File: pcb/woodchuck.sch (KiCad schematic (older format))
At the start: 5 parts, among them IC101 ADP3335, P101 CONN_01X02

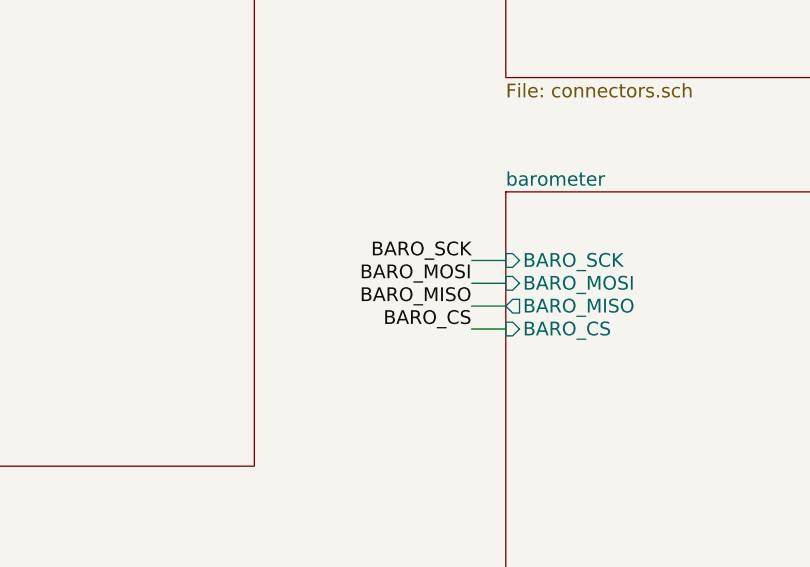
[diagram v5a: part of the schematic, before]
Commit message: Fix barometer hierarchical pins and add Farnell numbers to components
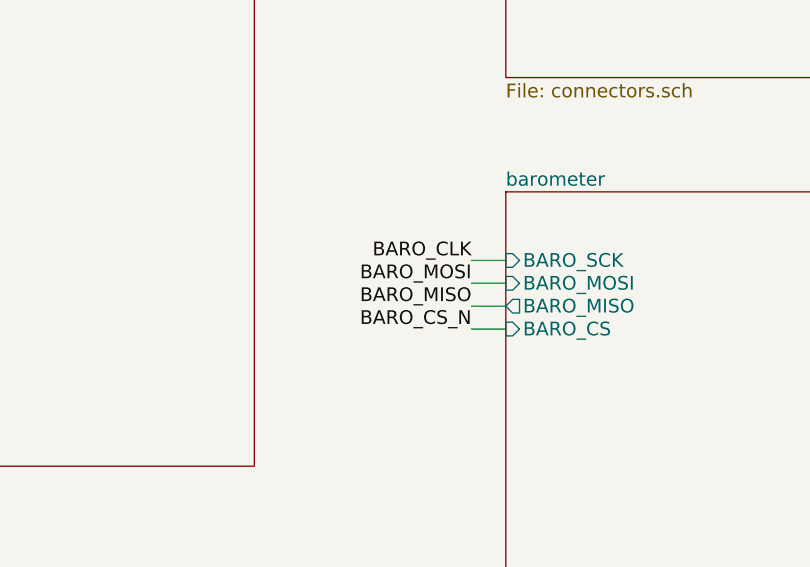
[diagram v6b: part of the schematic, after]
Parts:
- C101, C103: Farnell Value -> 2211185
- C102: Farnell Value -> 1759088
- IC101: Digikey (none) -> Value; Farnell (none) -> 2067775; Fieldname (none) -> Value
- P101: Digikey (none) -> Value; Farnell (none) -> 1830747; Fieldname (none) -> Value
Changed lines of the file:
@@
 F 2 "Woodchuck:MSOP8" H 5200 6850 60  0000 C CNN
 F 3 "" H 5600 6150 60  0000 C CNN
+F 4 "Value" H 5200 6550 60  0001 C CNN "Digikey"
+F 5 "2067775" H 5200 6550 60  0001 C CNN "Farnell"
+F 6 "Value" H 5200 6550 60  0001 C CNN "Fieldname"
 	1    5200 6550
 	1    0    0    -1
@@
 F 3 "" H 5850 6700 60  0000 C CNN
 F 4 "Value" H 5850 6700 60  0001 C CNN "Digikey"
-F 5 "Value" H 5850 6700 60  0001 C CNN "Farnell"
+F 5 "1759088" H 5850 6700 60  0001 C CNN "Farnell"
 F 6 "Value" H 5850 6700 60  0001 C CNN "Fieldname"
 	1    5850 6700
@@
 F 3 "" H 6100 6700 60  0000 C CNN
 F 4 "Value" H 6100 6700 60  0001 C CNN "Digikey"
-F 5 "Value" H 6100 6700 60  0001 C CNN "Farnell"
+F 5 "2211185" H 6100 6700 60  0001 C CNN "Farnell"
 F 6 "Value" H 6100 6700 60  0001 C CNN "Fieldname"
 	1    6100 6700
@@
 F 3 "" H 4400 6700 60  0000 C CNN
 F 4 "Value" H 4400 6700 60  0001 C CNN "Digikey"
-F 5 "Value" H 4400 6700 60  0001 C CNN "Farnell"
+F 5 "2211185" H 4400 6700 60  0001 C CNN "Farnell"
 F 6 "Value" H 4400 6700 60  0001 C CNN "Fieldname"
 	1    4400 6700
@@
 F 2 "Woodchuck:S02B-PASK-2" V 4250 6650 60  0000 C CNN
 F 3 "" H 4000 6700 60  0000 C CNN
+F 4 "Value" H 4000 6700 60  0001 C CNN "Digikey"
+F 5 "1830747" H 4000 6700 60  0001 C CNN "Farnell"
+F 6 "Value" H 4000 6700 60  0001 C CNN "Fieldname"
 	1    4000 6700
 	-1   0    0    1
@@
 	7400 4600 7250 4600
 Text Label 7250 4300 2    60   ~ 0
-BARO_SCK
+BARO_CLK
 Text Label 7250 4400 2    60   ~ 0
 BARO_MOSI
@@
 BARO_MISO
 Text Label 7250 4600 2    60   ~ 0
-BARO_CS
+BARO_CS_N
 $EndSCHEMATC

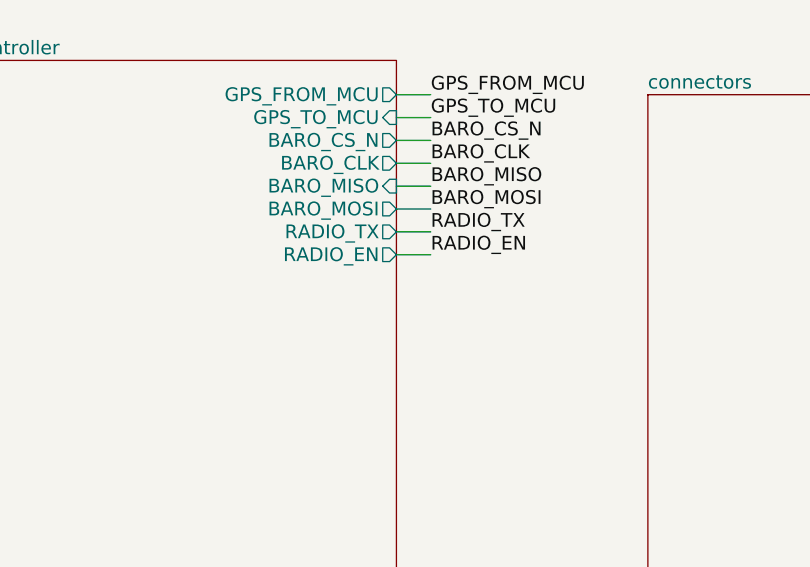
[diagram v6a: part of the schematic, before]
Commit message: Connect MTX2 parallel channel select pins to the MCU
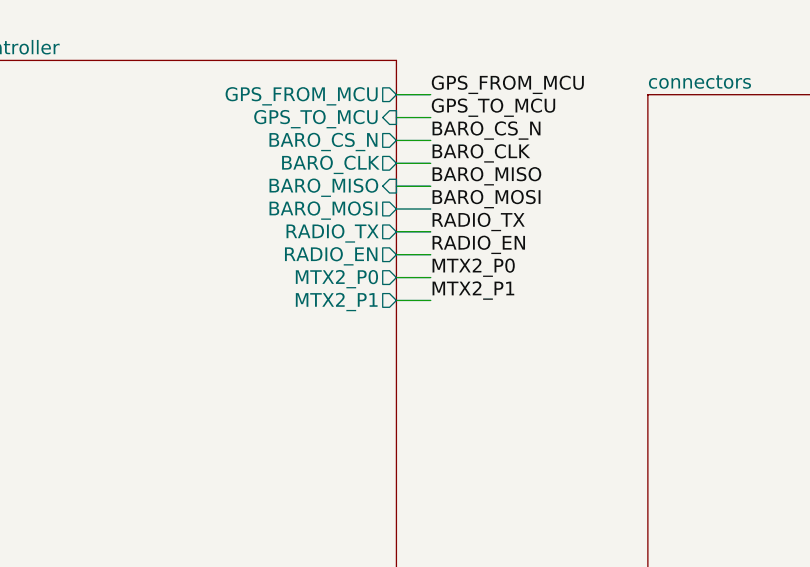
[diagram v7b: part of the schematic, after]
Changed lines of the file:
@@
 F8 "RADIO_TX" O R 6300 1900 60
 F9 "RADIO_EN" O R 6300 2000 60
+F10 "MTX2_P1" O R 6300 2200 60
+F11 "MTX2_P0" O R 6300 2100 60
 $EndSheet
 $Sheet
@@
 	1    0    0    -1
 $EndComp
-Wire Notes Line
-	3850 7250 6450 7250
-Wire Notes Line
-	6450 7250 6450 5900
-Wire Notes Line
-	6450 5900 3850 5900
-Wire Wire Line
-	4200 6550 4850 6550
-Wire Notes Line
-	3850 5900 3850 7250
-Wire Wire Line
-	5550 6450 5700 6450
-Wire Wire Line
-	5700 6450 5700 6650
-Wire Wire Line
-	5700 6650 5550 6650
-Connection ~ 5700 6550
-Wire Wire Line
-	5550 6750 5650 6750
-Wire Wire Line
-	5650 6750 5650 6850
-Wire Wire Line
-	5650 6850 5850 6850
-Connection ~ 5850 6550
-Wire Wire Line
-	4850 6750 4750 6750
-Wire Wire Line
-	4750 6750 4750 6850
-Wire Wire Line
-	4750 6850 4200 6850
-Wire Wire Line
-	5850 6550 5850 6450
-Wire Wire Line
-	5550 6550 6100 6550
-Wire Wire Line
-	4750 6650 4850 6650
-Wire Wire Line
-	4750 6450 4750 6650
-Connection ~ 4750 6550
-Wire Wire Line
-	4200 6750 4200 6900
-Wire Wire Line
-	4200 6650 4200 6550
-Wire Wire Line
-	4750 6450 4850 6450
-Connection ~ 4200 6850
-Connection ~ 4400 6850
-Connection ~ 4400 6550
-Connection ~ 4200 6550
-Wire Wire Line
-	3400 1500 3550 1500
-Wire Wire Line
-	3400 1600 3550 1600
 Text Label 3550 1500 0    60   ~ 0
 GPS_FROM_MCU
 Text Label 3550 1600 0    60   ~ 0
 GPS_TO_MCU
-Wire Wire Line
-	6300 1300 6450 1300
-Wire Wire Line
-	6300 1400 6450 1400
-Wire Wire Line
-	6300 1500 6450 1500
-Wire Wire Line
-	6300 1600 6450 1600
-Wire Wire Line
-	6300 1700 6450 1700
-Wire Wire Line
-	6300 1800 6450 1800
-Wire Wire Line
-	6300 1900 6450 1900
-Wire Wire Line
-	6300 2000 6450 2000
 Text Label 6450 1300 0    60   ~ 0
 GPS_FROM_MCU
@@
 Text Label 6450 2000 0    60   ~ 0
 RADIO_EN
-Wire Wire Line
-	3400 5000 3550 5000
-Wire Wire Line
-	3400 5150 3550 5150
-Wire Wire Line
-	3400 5300 3550 5300
-Wire Wire Line
-	3400 5450 3550 5450
 Text Label 3550 5000 0    60   ~ 0
 MTX2_P0
@@
 Text Label 3550 5450 0    60   ~ 0
 RADIO_EN
-Wire Wire Line
-	7400 4300 7250 4300
-Wire Wire Line
-	7400 4400 7250 4400
-Wire Wire Line
-	7400 4500 7250 4500
-Wire Wire Line
-	7400 4600 7250 4600
 Text Label 7250 4300 2    60   ~ 0
 BARO_CLK
@@
 Text Label 7250 4600 2    60   ~ 0
 BARO_CS_N
+Wire Notes Line
+	3850 7250 6450 7250
+Wire Notes Line
+	6450 7250 6450 5900
+Wire Notes Line
+	6450 5900 3850 5900
+Wire Wire Line
+	4200 6550 4850 6550
+Wire Notes Line
+	3850 5900 3850 7250
+Wire Wire Line
+	5550 6450 5700 6450
+Wire Wire Line
+	5700 6450 5700 6650
+Wire Wire Line
+	5700 6650 5550 6650
+Connection ~ 5700 6550
+Wire Wire Line
+	5550 6750 5650 6750
+Wire Wire Line
+	5650 6750 5650 6850
+Wire Wire Line
+	5650 6850 5850 6850
+Connection ~ 5850 6550
+Wire Wire Line
+	4850 6750 4750 6750
+Wire Wire Line
+	4750 6750 4750 6850
+Wire Wire Line
+	4750 6850 4200 6850
+Wire Wire Line
+	5850 6550 5850 6450
+Wire Wire Line
+	5550 6550 6100 6550
+Wire Wire Line
+	4750 6650 4850 6650
+Wire Wire Line
+	4750 6450 4750 6650
+Connection ~ 4750 6550
+Wire Wire Line
+	4200 6750 4200 6900
+Wire Wire Line
+	4200 6650 4200 6550
+Wire Wire Line
+	4750 6450 4850 6450
+Connection ~ 4200 6850
+Connection ~ 4400 6850
+Connection ~ 4400 6550
+Connection ~ 4200 6550
+Wire Wire Line
+	3400 1500 3550 1500
+Wire Wire Line
+	3400 1600 3550 1600
+Wire Wire Line
+	6300 1300 6450 1300
+Wire Wire Line
+	6300 1400 6450 1400
+Wire Wire Line
+	6300 1500 6450 1500
+Wire Wire Line
+	6300 1600 6450 1600
+Wire Wire Line
+	6300 1700 6450 1700
+Wire Wire Line
+	6300 1800 6450 1800
+Wire Wire Line
+	6300 1900 6450 1900
+Wire Wire Line
+	6300 2000 6450 2000
+Wire Wire Line
+	3400 5000 3550 5000
+Wire Wire Line
+	3400 5150 3550 5150
+Wire Wire Line
+	3400 5300 3550 5300
+Wire Wire Line
+	3400 5450 3550 5450
+Wire Wire Line
+	7400 4300 7250 4300
+Wire Wire Line
+	7400 4400 7250 4400
+Wire Wire Line
+	7400 4500 7250 4500
+Wire Wire Line
+	7400 4600 7250 4600
+Wire Wire Line
+	6300 2100 6450 2100
+Wire Wire Line
+	6300 2200 6450 2200
+Text Label 6450 2100 0    60   ~ 0
+MTX2_P0
+Text Label 6450 2200 0    60   ~ 0
+MTX2_P1
 $EndSCHEMATC
